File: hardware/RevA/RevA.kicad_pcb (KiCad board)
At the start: 4 copper layers, 85 x 54 mm, 145 parts, among them J1 USB_C_Receptacle_USB2.0, J2 DNP Conn_02x02_Odd_Even, J3 DNP Conn_01x02, J4 DNP Conn_02x03_Odd_Even, J5 DNP Conn_01x02, SW1 SW_Push, SW2 SW_Push, U1 SY8120B1ABC, U10 SPI RAM LY68L6400SLIT, U2 XC6206P25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

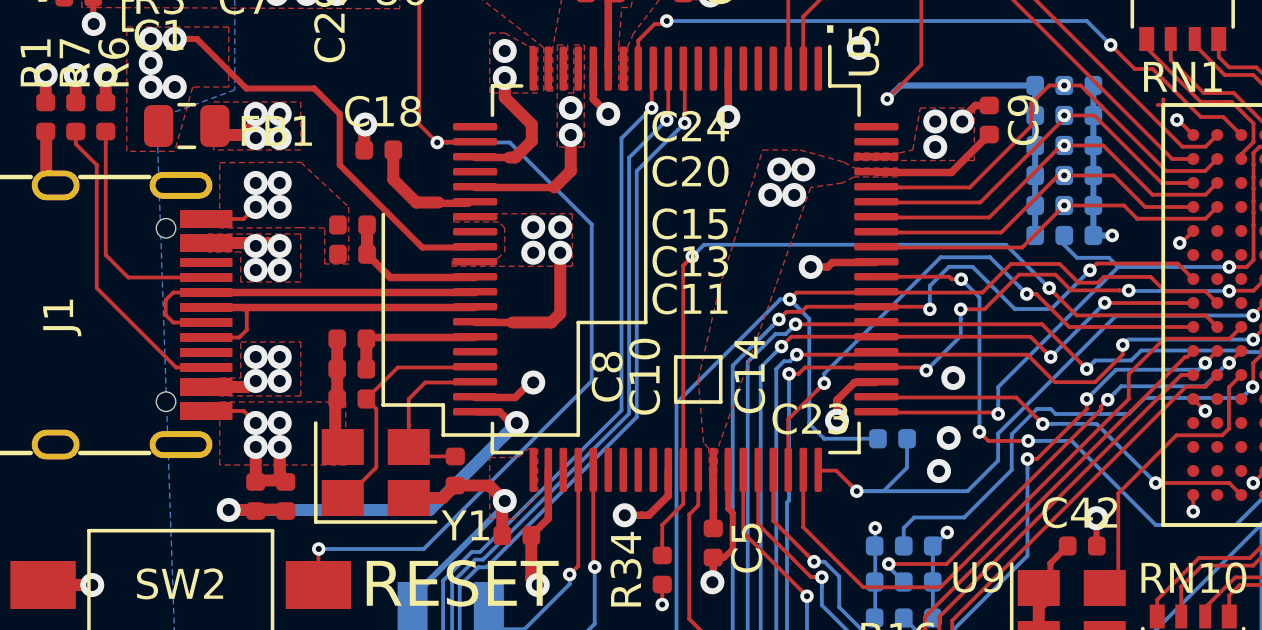
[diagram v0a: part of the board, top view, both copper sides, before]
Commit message: hardware: Add USB TH pads solderpaste layer
This was not being done before, leading to
stencils missing the through-hole pads for
the USB connector.
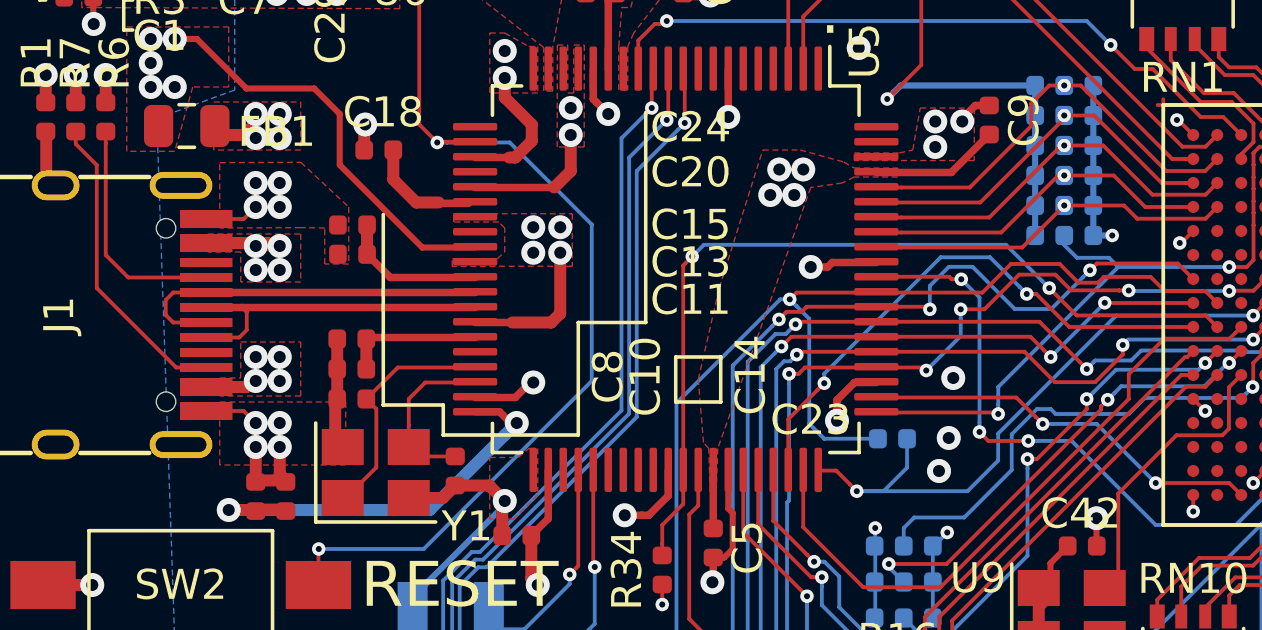
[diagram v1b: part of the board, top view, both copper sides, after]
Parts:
- R20, R21, R22, R25, R26, R27, R28, R29, R30, R31, R32: value 4K7 -> 10K
